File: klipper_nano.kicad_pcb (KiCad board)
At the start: 2 copper layers, 59.8 x 88.9 mm, 44 parts, among them J1 UART1, J10 SPI, J2 PWR_IN, J3 TFT, J4 USB_A, J5 USB_A, J6 SPI_PWR, J7 USB_B_Mini, J8 UART2, J9 PWC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

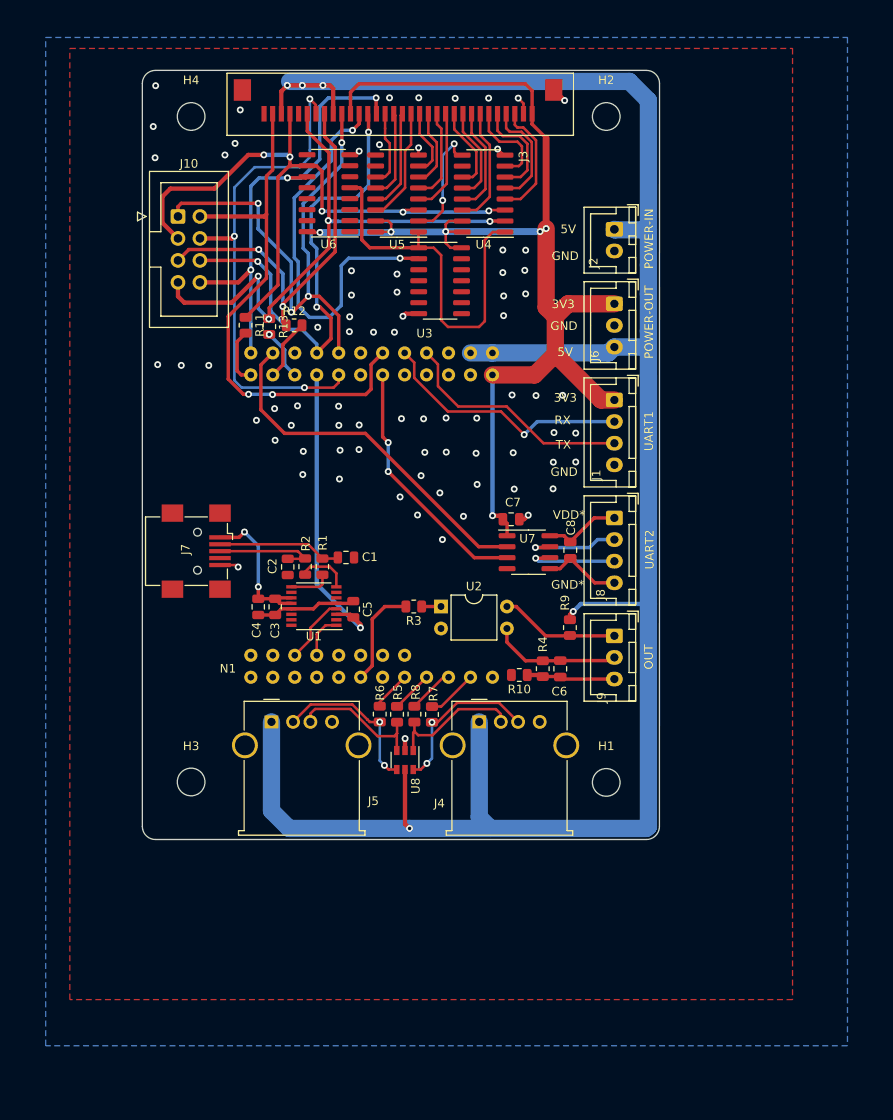
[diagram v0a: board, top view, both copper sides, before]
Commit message: Разъем под акселерометр Блок. конденсаторы Управление подстветкой экрана
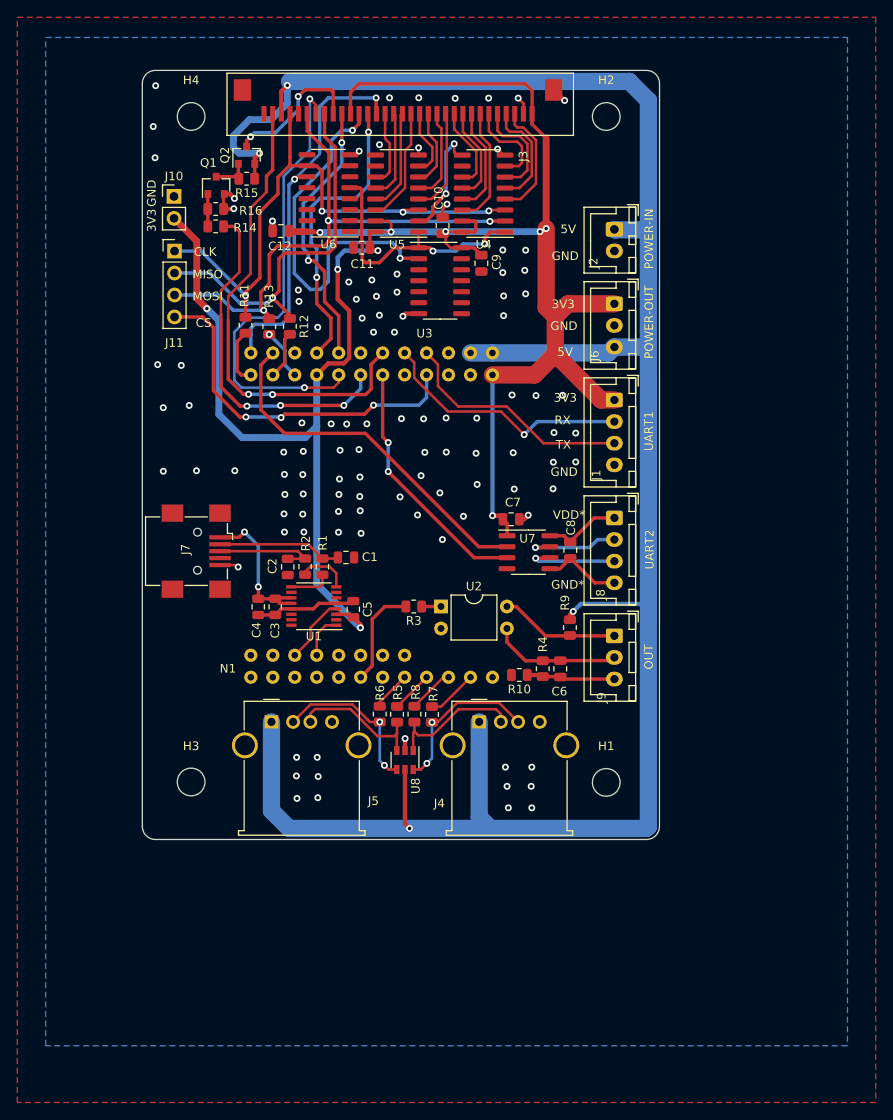
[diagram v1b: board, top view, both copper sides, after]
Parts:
- added C10: 0.1uF, Capacitor_SMD:C_0805_2012Metric, F.Cu at (102.1, 52.6)
- added C11: 0.1uF, Capacitor_SMD:C_0805_2012Metric, F.Cu at (92.7, 55.2)
- added C12: 0.1uF, Capacitor_SMD:C_0805_2012Metric, F.Cu at (83.4, 53.2)
- added C9: 0.1uF, Capacitor_SMD:C_0805_2012Metric, F.Cu at (106.6, 57.0)
- added J11: ACC_SPI, Connector_PinHeader_2.54mm:PinHeader_1x04_P2.54mm_Vertical, F.Cu at (71.1, 55.6)
- added Q1: IRLML6344TRPBF, Package_TO_SOT_SMD:SOT-23, F.Cu at (75.9, 48.0)
- added Q2: IRLML6402, Package_TO_SOT_SMD:SOT-23, F.Cu at (79.4, 44.5)
- added R14: 100, Resistor_SMD:R_0805_2012Metric, F.Cu at (75.8, 52.7)
- added R15: 10K, Resistor_SMD:R_0805_2012Metric, F.Cu at (79.4, 47.2)
- added R16: 10K, Resistor_SMD:R_0805_2012Metric, F.Cu at (75.8, 50.7)
- J10: value SPI -> ACC_PWR; footprint Connector_IDC:IDC-Header_2x04_P2.54mm_Vertical -> Connector_PinHeader_2.54mm:PinHeader_1x02_P2.54mm_Vertical
- J6: value SPI_PWR -> PWR_OUT
- moved J10 2.37 mm to (71.0, 49.2)
- moved R12 0.50 mm to (84.4, 64.3), turned to 270 degrees
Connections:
- J10 pad 1: /RST -> GND
- J10 pad 2: /TOUCH_CS -> 3V3
- J3 pad 24: 5V -> /16bit2SPI/TFT_LED
- N1 pad 38: (no net) -> /LCD_LED
- N1 pad 41: (no net) -> /ACC_CS
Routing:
- net 3V3: track 176.0 -> 246.9 mm, vias 7 -> 10
- net /ACC_CS: track 0.00 -> 41.8 mm, vias 0 -> 3
- net /LCD_LED: track 0.00 -> 40.4 mm, vias 0 -> 3
- net /RST: track 59.4 -> 31.6 mm, vias 4 -> 2
- net /DC: track 55.7 -> 34.5 mm, vias 3 -> 2
- net /16bit2SPI/TFT_LED: track 0.00 -> 16.7 mm, vias 0 -> 2
- net Net-(U3-Pad1): track 44.3 -> 30.3 mm, vias 0 -> 2
- net /CLK0: track 79.9 -> 67.9 mm, vias 5 -> 4
- net 5V: track 248.0 -> 258.6 mm, vias 5 -> 4
- net /CS0: track 52.2 -> 44.0 mm, vias 3 -> 2
- net /TOUCH_CS: track 62.9 -> 55.1 mm
- net GND: track 25.5 -> 32.9 mm, vias 76 -> 108
- net /TOUCH_IRQ: track 58.8 -> 53.7 mm, vias 3 -> 2
- net Net-(Q1-Pad3): track 0.00 -> 4.47 mm
- net Net-(Q1-Pad1): track 0.00 -> 3.75 mm
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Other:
- board text added: "CLK"
- board text added: "CS"
- board text added: "MISO"
- board text added: "MOSI"

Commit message: v2
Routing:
- net /16bit2SPI/TFT_LED: track 16.7 -> 17.2 mm
